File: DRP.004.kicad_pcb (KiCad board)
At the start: 2 copper layers, 53.4 x 26.8 mm, 77 parts, among them J1 Conn_01x03_Pin, J2 USB_C_Receptacle_PowerOnly_6P, J3 Conn_01x03_Pin, J4 Conn_01x05_Pin, J5 Conn_01x03_Pin, J6 Conn_01x03_Pin, Q1 2N7002, Q2 2N7002, Q3 DTC143Z, Q4 2N7002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

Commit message: v2 Rev
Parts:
- removed R14, R15, R24: 100k, Resistor_SMD:R_0603_1608Metric
- J4, J5: moved to B.Cu
- Q4: value 2N7002 -> DTC143Z; footprint Package_TO_SOT_SMD:SOT-23 -> SOT-523:SOT-523
- TP6: footprint TestPoint:TestPoint_Loop_D3.80mm_Drill2.0mm -> Connector_PinSocket_2.54mm:PinSocket_1x01_P2.54mm_Vertical
- moved #G1 23.3 mm to (177.0, 70.3)
- moved C14 14.4 mm to (140.3, 55.3), turned to 180 degrees
- moved R19 10.9 mm to (144.4, 53.7), turned to 0 degrees
- moved Q4 7.20 mm to (142.5, 68.7), turned to 0 degrees
- moved R22 7.00 mm to (143.1, 66.3)
- moved C11 6.49 mm to (154.9, 57.3), turned to 0 degrees
- moved J4 6.06 mm to (147.9, 68.4)
- moved R23 5.62 mm to (129.0, 64.0), turned to 180 degrees
- moved R13 4.04 mm to (132.7, 62.3)
- moved TP7 3.86 mm to (132.4, 68.7)
- moved R16 3.20 mm to (129.7, 58.8)
- moved C9 3.15 mm to (133.5, 59.5)
- moved R17 3.15 mm to (132.0, 59.5)
- moved R20 3.14 mm to (129.0, 65.5), turned to 180 degrees
- moved C12 3.11 mm to (144.4, 50.7)
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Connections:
- TP10 pad 1: NRST -> GND
- TP4 pad 1: SWCLK -> SWDIO
- TP5 pad 1: GND -> NRST
- TP9 pad 1: SWDIO -> SWCLK
- U6 pad 14: unconnected-(U6-PB0-Pad14) -> CHRG
- U6 pad 15: EN_LDR -> PGOOD
- U6 pad 16: ADC_LDR -> unconnected-(U6-PA8-Pad16)
- U6 pad 18: PGOOD -> ADC_LDR
- U6 pad 19: CHRG -> EN_LDR
- U6 pad 25: EN_SERVO -> SERWO_PWM
- U6 pad 28: SERWO_PWM -> EN_SERVO
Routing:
- net +3V3: track 98.5 -> 76.6 mm, vias 2 -> 1
- net CHRG: track 42.8 -> 28.2 mm
- net SWCLK: track 9.09 -> 19.5 mm
- net PGOOD: track 37.1 -> 29.7 mm
- net LED_RED: track 18.7 -> 11.4 mm, vias 2 -> 0
- net Net-(D5-K): track 1.54 -> 8.51 mm
- net EN_SERVO: track 11.0 -> 5.66 mm
- net Net-(Q2-G): track 5.98 -> 1.69 mm
- net SWDIO: track 14.9 -> 10.6 mm
- net GND: track 5.94 -> 10.2 mm
- net Net-(D3-K): track 1.54 -> 5.23 mm
- net ADC_BATT: track 6.09 -> 9.70 mm
- net Net-(Q4-B): track 5.29 -> 1.89 mm
- net VSYS: track 94.7 -> 91.4 mm
- net ON_DETECT: track 15.1 -> 18.3 mm
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
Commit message: Removed C5 Improved layout
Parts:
- removed C5: 22uF, Capacitor_SMD:C_0603_1608Metric
- R19: value 100k -> 10k
- R20, R21, R23: value 100 -> 220
- moved R12 4.34 mm to (151.2, 54.1), turned to 0 degrees
- moved U5 1.48 mm to (153.4, 52.4)
- moved J3 1.47 mm to (155.8, 49.2)
- moved U4 1.47 mm to (153.4, 54.4)
- moved C15 1.32 mm to (151.2, 48.5)
- moved Q1 1.25 mm to (150.8, 51.6), turned to 180 degrees
- moved R18 0.51 mm to (144.9, 52.3)
- moved R19 0.51 mm to (144.9, 53.8)
- moved C12 0.51 mm to (144.9, 50.7)
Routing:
- net EN_SERVO: track 5.66 -> 8.27 mm
- net GND: track 10.2 -> 11.5 mm, vias 375 -> 368
- net SERWO_PWM: track 13.7 -> 14.3 mm
- net NRST: track 24.2 -> 24.8 mm

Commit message: Return of the duck!
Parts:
- #G1: moved to B.Cu
- moved #G1 54.9 mm to (122.3, 67.0), turned to 180 degrees
- moved TP7 0.92 mm to (133.3, 68.8)
- moved C13 0.05 mm to (143.4, 55.3)
- moved C12 0.05 mm to (144.9, 50.7)
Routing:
- net GND: vias 368 -> 375

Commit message: Made prettier look
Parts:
- TP6: footprint Connector_PinSocket_2.54mm:PinSocket_1x01_P2.54mm_Vertical -> Connector_PinHeader_2.54mm:PinHeader_1x01_P2.54mm_Vertical
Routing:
- net GND: track 11.5 -> 11.6 mm, vias 375 -> 376

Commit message: Some cleanup
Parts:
- moved Q4 0.76 mm to (143.1, 68.2)
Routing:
- net Net-(J6-Pin_1): track 6.11 -> 6.88 mm
- net GND: track 11.6 -> 12.3 mm, vias 376 -> 378

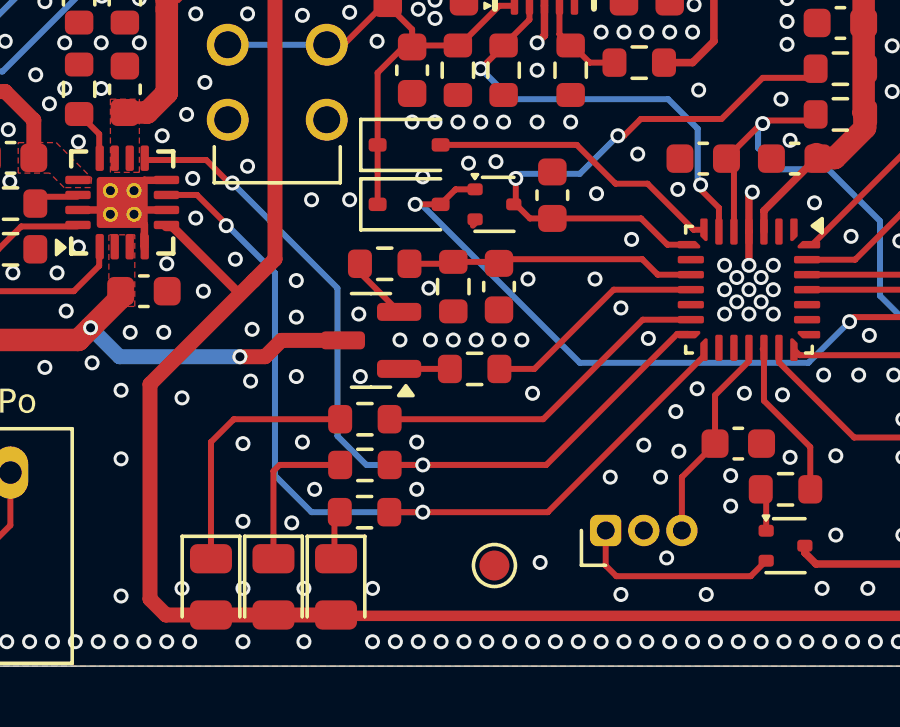
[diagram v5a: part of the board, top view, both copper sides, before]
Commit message: Beautify placements (R20 R21 R23)
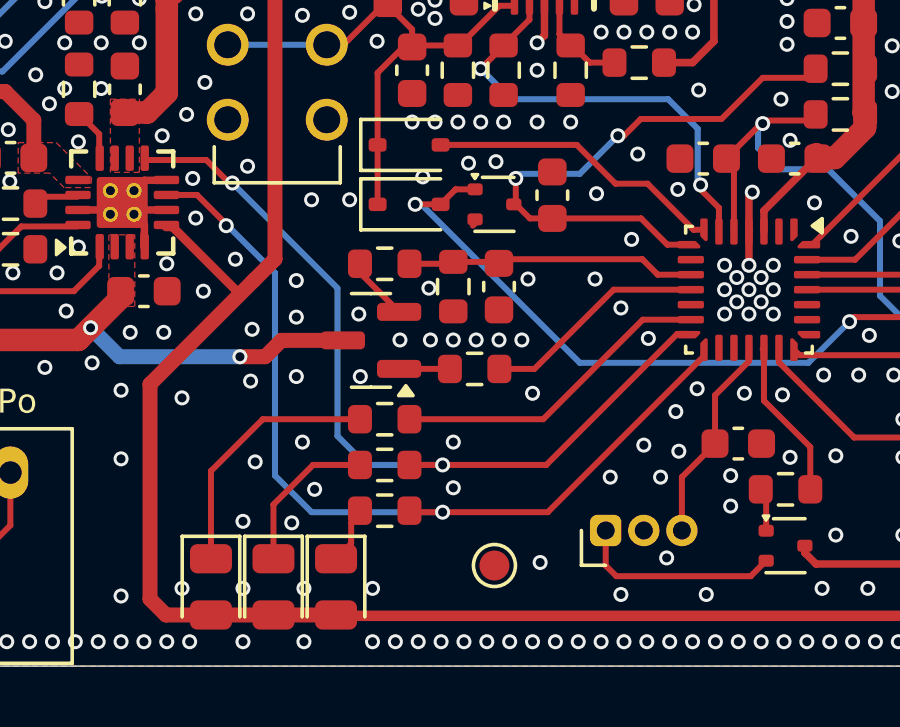
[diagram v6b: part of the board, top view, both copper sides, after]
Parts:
- moved R21 0.67 mm to (129.7, 67.0)
- moved R20 0.66 mm to (129.7, 65.5)
- moved R23 0.66 mm to (129.7, 64.0)
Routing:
- net LED_RED: track 11.4 -> 10.8 mm
